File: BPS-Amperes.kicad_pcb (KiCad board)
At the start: 2 copper layers, 58.2 x 30.2 mm, 46 parts, among them J1 ShuntConn, J2 LeaderConn, J3 Conn_01x04, U1 INA186A3IDDFT, U2 RO-123.3S_HP, U3 LTC6820, U4 HX1188FNL, U5 REF1930AIDDCT, U6 LTC2315, U7 OPA2196

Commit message: Update label
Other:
- board text added: "UTSVT - BPS Amperes Board v2.5 Fall 2021"
- board text removed: "UTSVT - BPS Amperes Board v2.4 Fall 2021"
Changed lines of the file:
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@@
     (effects (font (size 0.8 0.8) (thickness 0.15)))
   )
-  (gr_text "UTSVT - BPS\nAmperes Board v2.4\nFall 2021" (at 132.2 123.8) (layer "F.SilkS")
+  (gr_text "UTSVT - BPS\nAmperes Board v2.5\nFall 2021" (at 132.2 123.8) (layer "F.SilkS")
     (effects (font (size 1 1) (thickness 0.15)))
   )

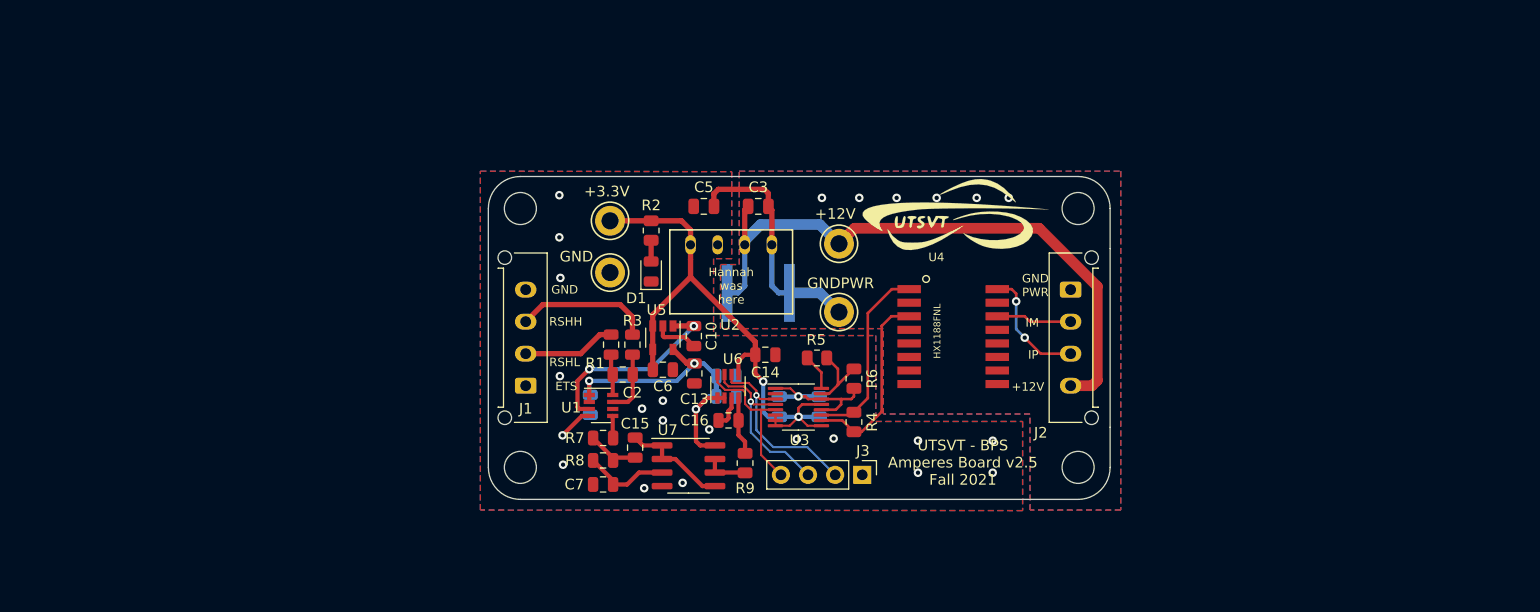
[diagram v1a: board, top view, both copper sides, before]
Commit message: layout with no pours
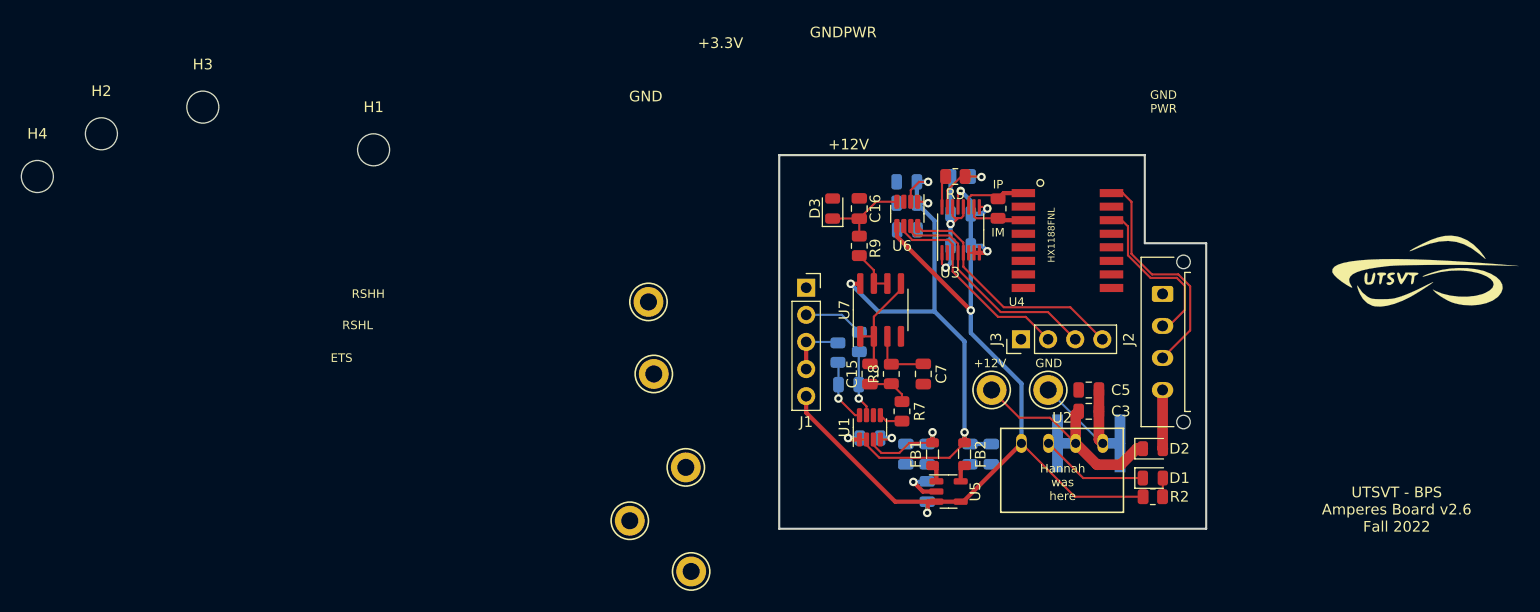
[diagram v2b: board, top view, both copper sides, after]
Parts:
- added C17: 100nF, Capacitor_SMD:C_0805_2012Metric, B.Cu at (128.9, 123.0)
- added C18: 1uF, Capacitor_SMD:C_0805_2012Metric, B.Cu at (134.9, 123.0)
- added D2: D_Schottky, Diode_SMD:D_0805_2012Metric, F.Cu at (150.0, 122.5)
- added D3: 3.0V±0.05, Diode_SMD:D_0805_2012Metric, F.Cu at (120.0, 100.0)
- added FB1: FerriteBead_Small, Inductor_SMD:L_0805_2012Metric, F.Cu at (129.4, 123.0)
- added FB2: FerriteBead_Small, Inductor_SMD:L_0805_2012Metric, F.Cu at (132.4, 123.0)
- added TP5: Ain_TP, TestPoint:TestPoint_Keystone_5005-5009_Compact, F.Cu at (102.8, 108.8)
- added TP6: +1V5_TP, TestPoint:TestPoint_Keystone_5005-5009_Compact, F.Cu at (101.0, 129.2)
- added TP7: +3V0_TP, TestPoint:TestPoint_Keystone_5005-5009_Compact, F.Cu at (103.2, 115.5)
- C10: value 100nF -> 1uF; moved to B.Cu
- C13, C14, C2, C6, R1, R3, R6: moved to B.Cu
- J1: footprint Connector_Molex:Molex_Micro-Fit_3.0_43650-0415_1x04_P3.00mm_Vertical -> Connector_PinSocket_2.54mm:PinSocket_1x05_P2.54mm_Vertical
- moved H2 91.8 mm to (51.5, 93.0)
- moved H3 88.7 mm to (61.0, 90.5)
- moved R2 53.2 mm to (150.0, 127.0), turned to 0 degrees
- moved H4 52.8 mm to (45.5, 97.0)
- moved D1 50.8 mm to (150.0, 125.2), turned to 0 degrees
- moved LOGO2 44.3 mm to (175.2, 106.0)
- moved C5 40.0 mm to (144.0, 117.0)
- moved C3 36.4 mm to (144.0, 119.0)
- moved U2 36.2 mm to (141.5, 122.0)
- moved C1 34.0 mm to (144.0, 122.0)
- moved TP3 33.7 mm to (106.8, 134.0), turned to 0 degrees
- moved C7 31.7 mm to (128.5, 115.5), turned to -90 degrees
- moved U5 30.4 mm to (130.9, 126.5), turned to 0 degrees
- moved LOGO1 29.1 mm to (159.5, 121.0)
- moved R8 28.2 mm to (125.5, 115.5), turned to 90 degrees
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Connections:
- C2 pad 1: /RSHL -> /RSHH
- C2 pad 2: /RSHH -> /RSHL
- J1 pad 2: GND -> Net-(J1-Pad2)
- J1 pad 3: Net-(J1-Pad3) -> GND
- J2 pad 4: +12V -> /+12V_In
- R1 pad 1: /RSHL -> /RSHH
- R1 pad 2: GND -> Net-(J1-Pad2)
- R3 pad 1: /RSHH -> /RSHL
- R3 pad 2: Net-(J1-Pad3) -> GND
- U5 pad 1: +1V5 -> Net-(FB1-Pad1)
- U5 pad 5: +3V0 -> Net-(FB2-Pad1)
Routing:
- net +12V: track 58.7 -> 22.1 mm
- net +3V3: track 55.6 -> 87.5 mm, vias 2 -> 5
- net +3V0: track 31.3 -> 59.3 mm, vias 3 -> 5
- net Net-(J1-Pad3): track 12.8 -> 0.00 mm
- net /IM: track 17.9 -> 5.67 mm
- net /IP: track 17.8 -> 6.44 mm
- net Net-(J2-Pad3): track 11.3 -> 21.6 mm, vias 2 -> 0
- net Net-(J2-Pad2): track 7.08 -> 16.0 mm
- net GNDPWR: track 22.7 -> 13.9 mm, vias 6 -> 0
- net /CS: track 14.7 -> 23.0 mm
- net +1V5: track 18.6 -> 11.0 mm, vias 2 -> 1
- net Net-(J1-Pad2): track 0.00 -> 5.65 mm
- net /+12V_In: track 0.00 -> 5.51 mm
- net /SCK: track 16.7 -> 21.5 mm, vias 1 -> 0
- net Net-(C16-Pad1): track 5.44 -> 8.33 mm
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- removed copper zone on B.Cu, net GND
- removed copper zone on F.Cu, net GND
- removed copper zone on B.Cu, net GNDPWR
- removed copper zone on F.Cu, net GNDPWR
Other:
- board size 58.2 x 30.2 mm -> 40 x 35 mm
- board text added: "UTSVT - BPS Amperes Board v2.6 Fall 2022"
- board text removed: "UTSVT - BPS Amperes Board v2.5 Fall 2021"

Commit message: add 👈 pass 💦 through 🐲 connector
and move 📦 things 🍄 around ➕🏜️➡️👤 a bit 😁
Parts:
- removed H1, H2, H3, H4: M3, MountingHole:MountingHole_3mm
- added J4: Conn_01x05, Connector_PinHeader_2.54mm:PinHeader_1x05_P2.54mm_Vertical, F.Cu at (152.5, 107.4)
- C2, R1, R3: moved to F.Cu
- D2, LOGO2: moved to B.Cu
- TP1, TP2: footprint TestPoint:TestPoint_Keystone_5005-5009_Compact -> TestPoint:TestPoint_Pad_2.0x2.0mm
- TP3, TP4, TP6, TP7: footprint TestPoint:TestPoint_Keystone_5005-5009_Compact -> TestPoint:TestPoint_Pad_1.5x1.5mm
- TP5: footprint TestPoint:TestPoint_Keystone_5005-5009_Compact -> Connector_PinSocket_2.54mm:PinSocket_1x01_P2.54mm_Vertical
- moved LOGO1 35.0 mm to (125.8, 111.8)
- moved LOGO2 34.9 mm to (141.5, 115.0), turned to 180 degrees
- moved U5 28.4 mm to (124.0, 99.0), turned to 180 degrees
- moved C6 27.7 mm to (126.0, 99.0), turned to -90 degrees
- moved TP5 26.8 mm to (129.2, 112.5)
- moved C18 25.3 mm to (120.0, 102.5), turned to 90 degrees
- moved C13 23.2 mm to (122.0, 102.5), turned to 90 degrees
- moved C1 23.0 mm to (145.0, 99.0), turned to 180 degrees
- moved FB2 22.8 mm to (122.5, 102.5), turned to -90 degrees
- moved TP6 21.7 mm to (122.5, 126.5)
- moved J2 21.2 mm to (139.5, 125.9), turned to 180 degrees
- moved FB1 20.9 mm to (125.5, 102.5), turned to -90 degrees
- moved C17 20.7 mm to (126.0, 102.5), turned to 90 degrees
- moved C10 20.5 mm to (128.0, 102.5), turned to 90 degrees
- moved TP7 20.5 mm to (120.5, 126.5)
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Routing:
- net GNDPWR: track 13.9 -> 44.8 mm, vias 0 -> 1
- net +3V3: track 87.5 -> 108.0 mm, vias 5 -> 4
- net +1V5: track 11.0 -> 29.5 mm, vias 1 -> 2
- net +12V: track 22.1 -> 39.8 mm, vias 0 -> 1
- net GND: track 35.4 -> 49.1 mm, vias 4 -> 15
- net /+12V_In: track 5.51 -> 15.8 mm
- net Net-(J2-Pad2): track 16.0 -> 8.86 mm
- net /IP: track 6.44 -> 12.6 mm
- net Net-(J2-Pad3): track 21.6 -> 15.5 mm
- net +3V0: track 59.3 -> 53.6 mm, vias 5 -> 3
- net /CS: track 23.0 -> 18.0 mm, vias 0 -> 1
- net Net-(C16-Pad1): track 8.33 -> 11.7 mm
- net /SCK: track 21.5 -> 18.5 mm, vias 0 -> 1
- net /IM: track 5.67 -> 8.54 mm
- net Net-(J1-Pad2): track 5.65 -> 7.53 mm
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- added copper zone on B.Cu, net GND
- added copper zone on F.Cu, net GND
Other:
- outline, holes or cut-outs redrawn
- board text added: "1v5"
- board text added: "3v0"
- board text added: "3v3"
- board text removed: "+3.3V"
- board text removed: "GNDPWR"
